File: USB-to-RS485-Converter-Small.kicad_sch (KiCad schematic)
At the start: 21 parts, among them IC1 SN65HVD1782D, J1 Conn_01x02_Pin, J2 USB_B, J3 DE9_Plug_MountingHoles, U1 FT232RL

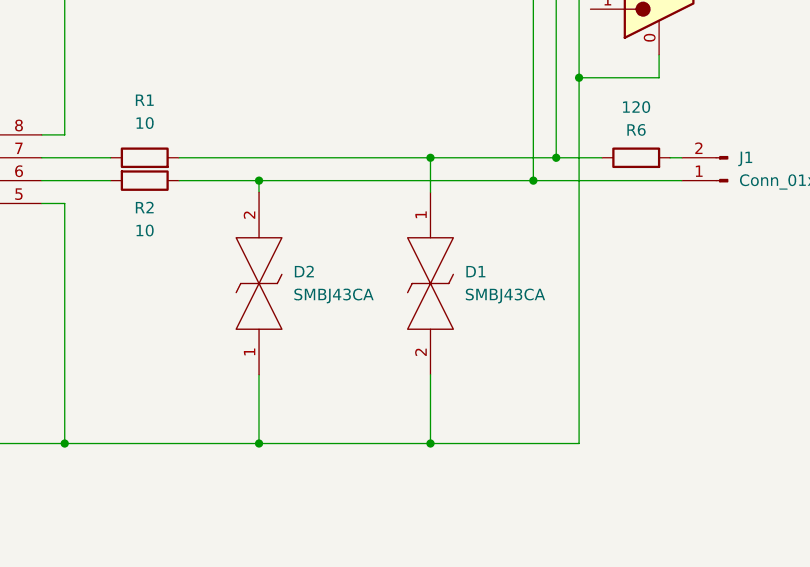
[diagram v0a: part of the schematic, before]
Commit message: Changed TVS diode
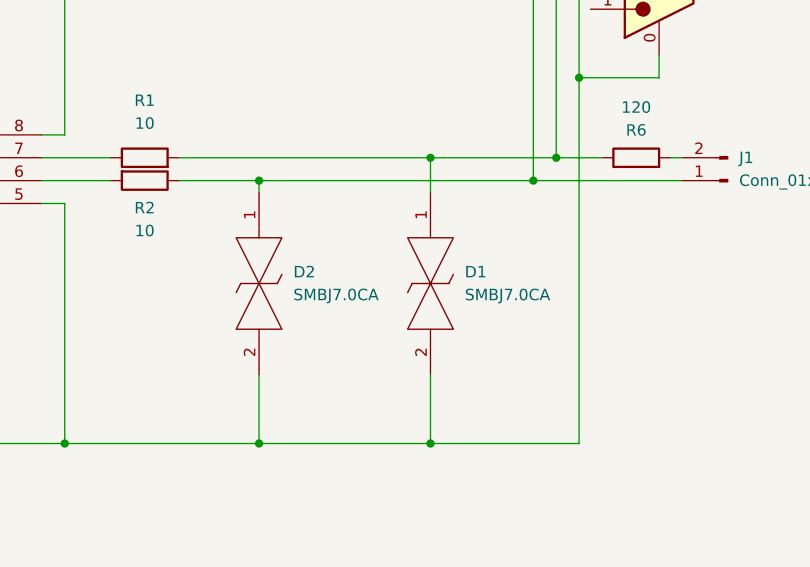
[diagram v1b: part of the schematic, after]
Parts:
- removed D1, D2: SMBJ43CA, DIONM5436X261N, symbol SamacSys_Parts:SMBJ43CA
- added D1, D2: SMBJ7.0CA, DIONM5436X261N, symbol SamacSys_Parts:SMBJ7.0CA
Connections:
- net GND: now also D1.2, D2.2
- net at J1.1 (Pin_1), J3.3, R2.1: now also D2.1
- net at J3.7, R1.2, R6.1: now also D1.1

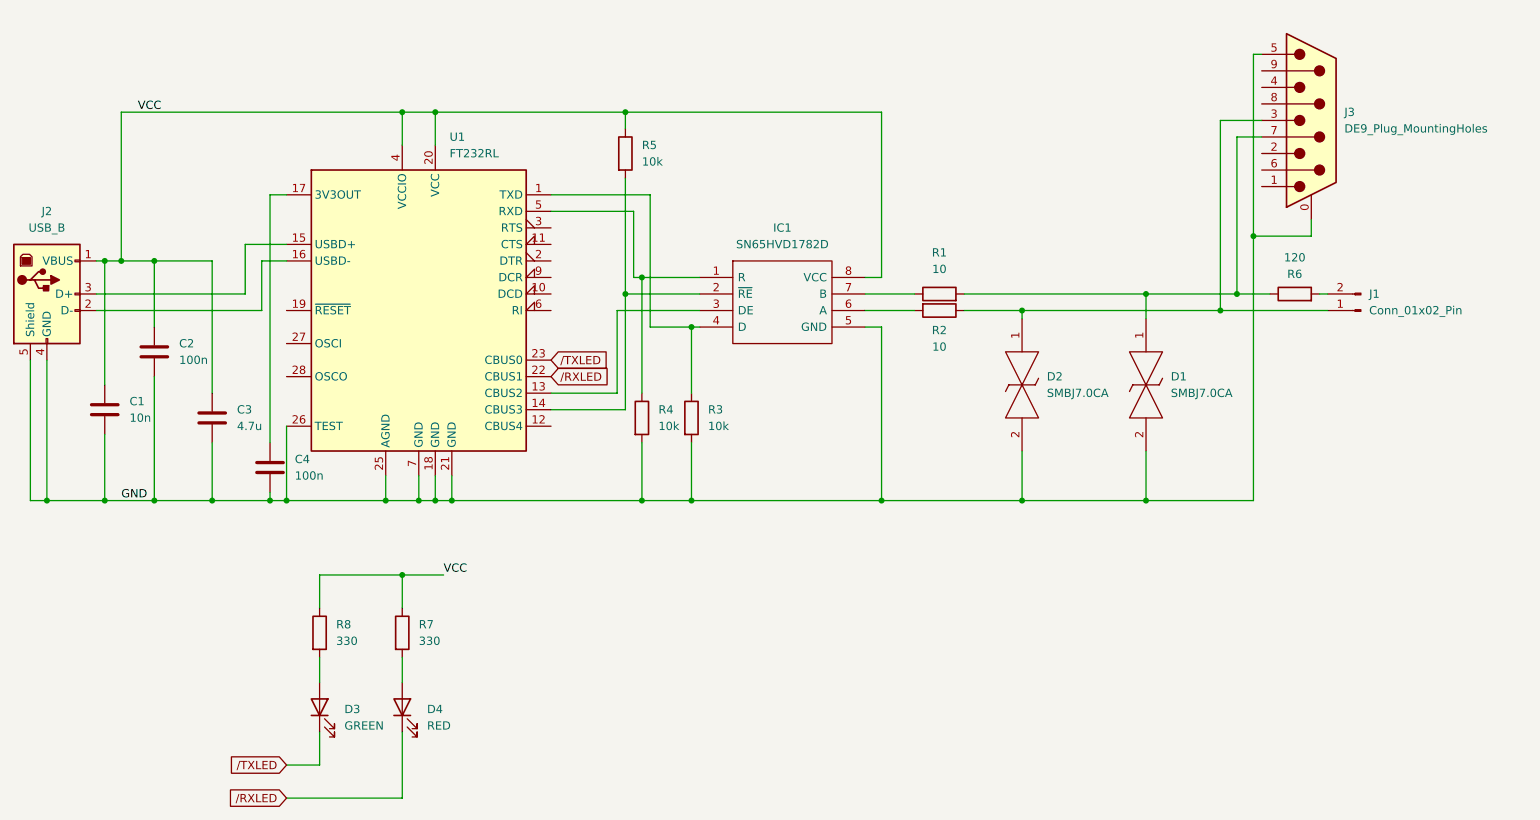
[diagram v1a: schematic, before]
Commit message: Changed RS485 transceiver and TVS diode
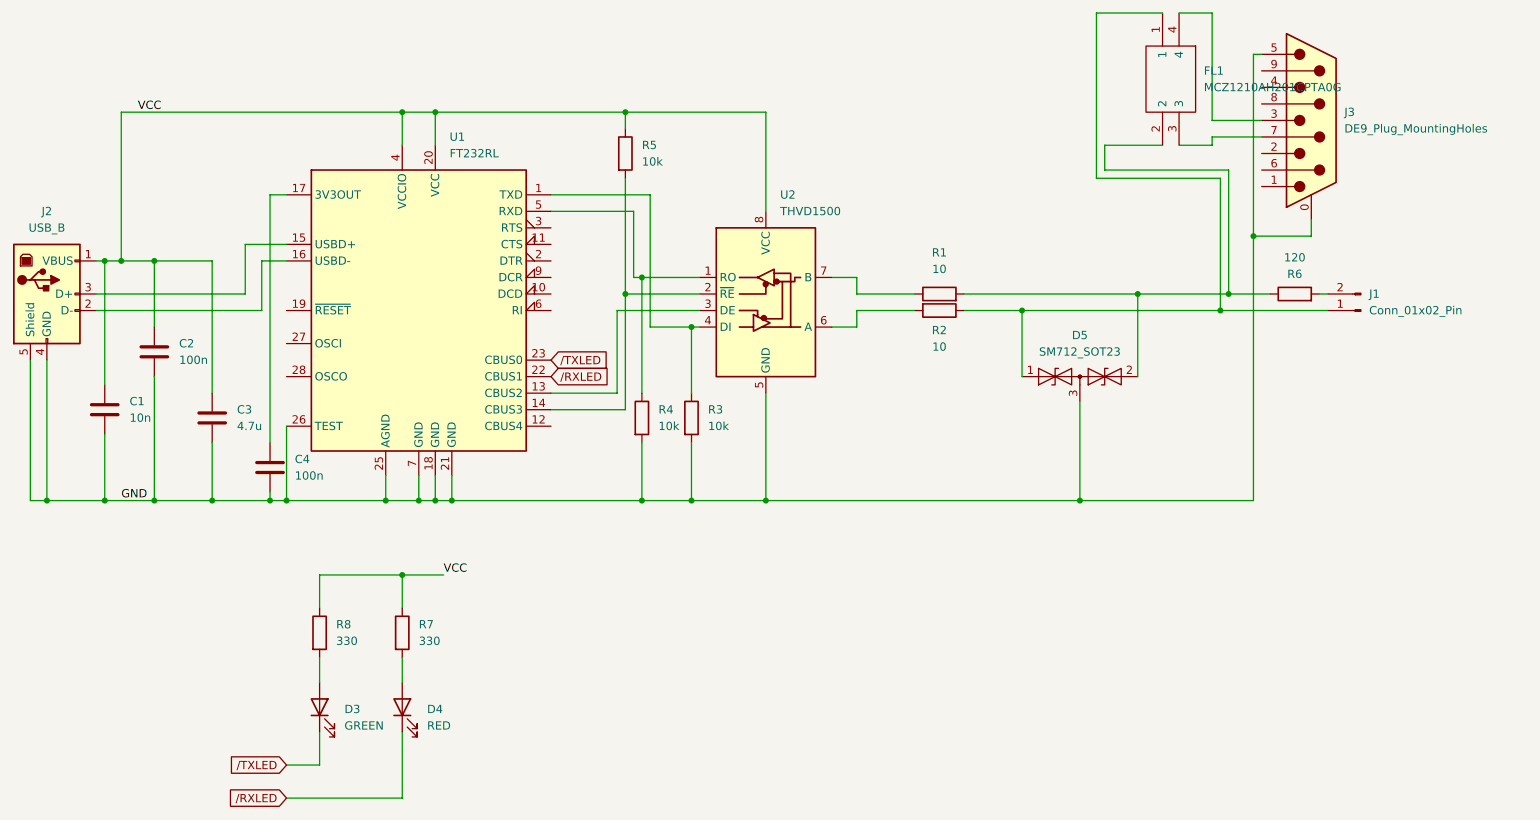
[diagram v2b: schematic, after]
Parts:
- removed D1, D2: SMBJ7.0CA, DIONM5436X261N, symbol SamacSys_Parts:SMBJ7.0CA
- removed IC1: SN65HVD1782D, SOIC127P600X175-8N, symbol SamacSys_Parts:SN65HVD1782D
- added D5: SM712_SOT23, Package_TO_SOT_SMD:SOT-23, symbol Diode:SM712_SOT23
- added FL1: MCZ1210AH201CPTA0G, MCZ1210AH201CPTA0G, symbol SamacSys_Parts:MCZ1210AH201CPTA0G
- added U2: THVD1500, Package_SO:SOIC-8_3.9x4.9mm_P1.27mm, symbol Interface_UART:THVD1500
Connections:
- net GND: now also D5.3 (common), U2.5 (GND)
- net VCC: now also U2.8 (VCC)
- net at J1.1 (Pin_1), R2.1: now also D5.1 (A1), FL1.1; no longer J3.3
- net at R1.2, R6.1: now also D5.2 (A2), FL1.2; no longer J3.7
- net at R1.1: now also U2.7 (B)
- net at R3.1, U1.1 (TXD): now also U2.4 (DI)
- net at U1.13 (CBUS2): now also U2.3 (DE)
- net at R5.2, U1.14 (CBUS3): now also U2.2 (~{RE})
- net at R4.1, U1.5 (RXD): now also U2.1 (RO)
- net at R2.2: now also U2.6 (A)
- new net: FL1.4, J3.3
- new net: FL1.3, J3.7

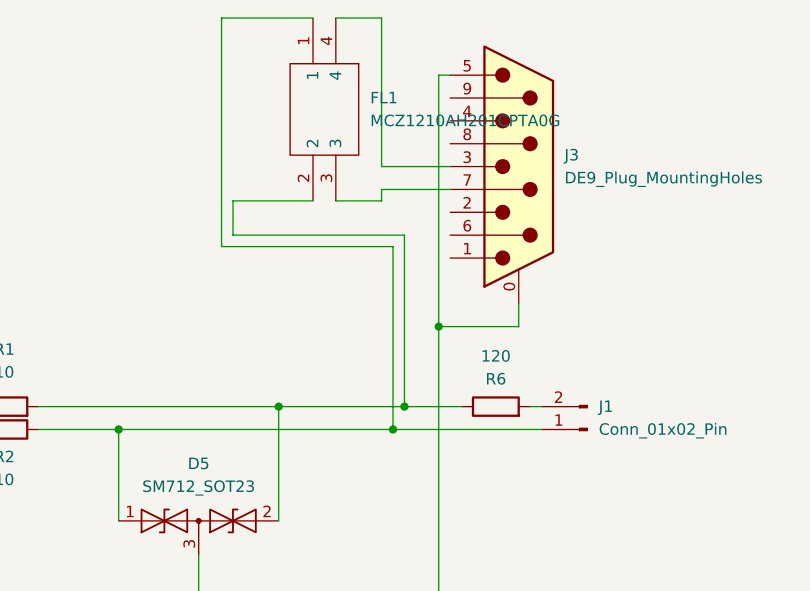
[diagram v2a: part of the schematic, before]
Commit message: Removed choke filter
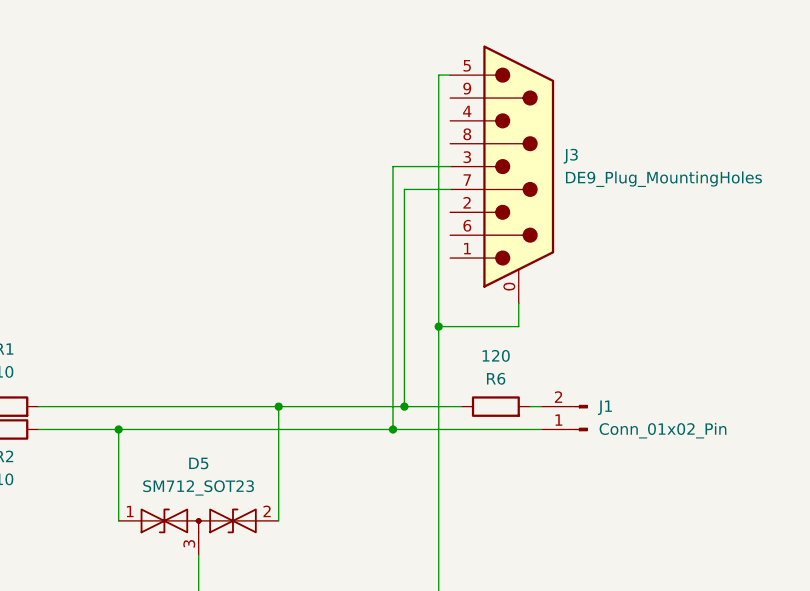
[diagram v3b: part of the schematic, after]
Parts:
- removed FL1: MCZ1210AH201CPTA0G, MCZ1210AH201CPTA0G, symbol SamacSys_Parts:MCZ1210AH201CPTA0G
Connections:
- net at J3.3: now also D5.1 (A1), J1.1 (Pin_1), R2.1
- net at J3.7: now also D5.2 (A2), R1.2, R6.1
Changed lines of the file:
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@@
 	(wire
 		(pts
-			(xy 222.25 48.26) (xy 212.09 48.26)
+			(xy 231.14 64.77) (xy 237.49 64.77)
 		)
 		(stroke
@@
 	(wire
 		(pts
-			(xy 212.09 73.66) (xy 231.14 73.66)
-		)
-		(stroke
-			(width 0)
-			(type default)
-		)
-	)
-	(wire
-		(pts
 			(xy 149.86 123.19) (xy 161.29 123.19)
 		)
@@
 	(wire
 		(pts
-			(xy 229.87 67.31) (xy 229.87 68.58)
-		)
-		(stroke
-			(width 0)
-			(type default)
-		)
-	)
-	(wire
-		(pts
 			(xy 105.41 134.62) (xy 105.41 139.7)
 		)
@@
 	(wire
 		(pts
-			(xy 229.87 64.77) (xy 237.49 64.77)
-		)
-		(stroke
-			(width 0)
-			(type default)
-		)
-	)
-	(wire
-		(pts
 			(xy 138.43 106.68) (xy 138.43 93.98)
 		)
@@
 	(wire
 		(pts
-			(xy 213.36 68.58) (xy 213.36 72.39)
-		)
-		(stroke
-			(width 0)
-			(type default)
-		)
-	)
-	(wire
-		(pts
 			(xy 110.49 63.5) (xy 139.7 63.5)
 		)
@@
 	(wire
 		(pts
-			(xy 212.09 48.26) (xy 212.09 73.66)
+			(xy 231.14 64.77) (xy 231.14 93.98)
 		)
 		(stroke
@@
 	(wire
 		(pts
-			(xy 229.87 68.58) (xy 224.79 68.58)
-		)
-		(stroke
-			(width 0)
-			(type default)
-		)
-	)
-	(wire
-		(pts
 			(xy 92.71 139.7) (xy 92.71 134.62)
 		)
@@
 	(wire
 		(pts
-			(xy 231.14 73.66) (xy 231.14 93.98)
-		)
-		(stroke
-			(width 0)
-			(type default)
-		)
-	)
-	(wire
-		(pts
 			(xy 245.11 80.01) (xy 245.11 82.55)
 		)
@@
 	(wire
 		(pts
-			(xy 229.87 48.26) (xy 229.87 64.77)
-		)
-		(stroke
-			(width 0)
-			(type default)
-		)
-	)
-	(wire
-		(pts
 			(xy 138.43 93.98) (xy 151.13 93.98)
 		)
@@
 	(wire
 		(pts
-			(xy 213.36 72.39) (xy 232.41 72.39)
-		)
-		(stroke
-			(width 0)
-			(type default)
-		)
-	)
-	(wire
-		(pts
 			(xy 59.69 113.03) (xy 59.69 123.19)
 		)
@@
 	(wire
 		(pts
-			(xy 232.41 72.39) (xy 232.41 91.44)
+			(xy 232.41 67.31) (xy 232.41 91.44)
 		)
 		(stroke
@@
 	(wire
 		(pts
-			(xy 224.79 48.26) (xy 229.87 48.26)
-		)
-		(stroke
-			(width 0)
-			(type default)
-		)
-	)
-	(wire
-		(pts
 			(xy 149.86 96.52) (xy 149.86 106.68)
 		)
@@
 	(wire
 		(pts
-			(xy 237.49 67.31) (xy 229.87 67.31)
-		)
-		(stroke
-			(width 0)
-			(type default)
-		)
-	)
-	(wire
-		(pts
 			(xy 142.24 88.9) (xy 151.13 88.9)
 		)
@@
 	(wire
 		(pts
-			(xy 213.36 68.58) (xy 222.25 68.58)
+			(xy 232.41 67.31) (xy 237.49 67.31)
 		)
 		(stroke
@@
 					(unit 1)
 				)
-			)
-		)
-	)
-	(symbol
-		(lib_id "SamacSys_Parts:MCZ1210AH201CPTA0G")
-		(at 224.79 48.26 270)
-		(unit 1)
-		(exclude_from_sim no)
-		(in_bom yes)
-		(on_board yes)
-		(dnp no)
-		(fields_autoplaced yes)
-		(property "Reference" "FL1"
-			(at 228.6 57.1499 90)
-			(effects
-				(font
-					(size 1.27 1.27)
-				)
-				(justify left)
-			)
-		)
-		(property "Value" "MCZ1210AH201CPTA0G"
-			(at 228.6 59.6899 90)
-			(effects
-				(font
-					(size 1.27 1.27)
-				)
-				(justify left)
-			)
-		)
-		(property "Footprint" "MCZ1210AH201CPTA0G"
-			(at 227.33 64.77 0)
-			(effects
-				(font
-					(size 1.27 1.27)
-				)
-				(justify left)
-				(hide yes)
-			)
-		)
-		(property "Datasheet" "https://product.tdk.com/system/files/dam/doc/product/emc/emc/cmf_cmc/catalog/cmf_commercial_signal_mcz1210ah_en.pdf"
-			(at 224.79 64.77 0)
-			(effects
-				(font
-					(size 1.27 1.27)
-				)
-				(justify left)
-				(hide yes)
-			)
-		)
-		(property "Description" "Common Mode Filters / Chokes, |Z|=200? at 100MHz."
-			(at 222.25 64.77 0)
-			(effects
-				(font
-					(size 1.27 1.27)
-				)
-				(justify left)
-				(hide yes)
-			)
-		)
-		(property "Height" "0.6"
-			(at 219.71 64.77 0)
-			(effects
-				(font
-					(size 1.27 1.27)
-				)
-				(justify left)
-				(hide yes)
-			)
-		)
-		(property "Mouser Part Number" "810-MCZ1210AH201CA0G"
-			(at 217.17 64.77 0)
-			(effects
-				(font
-					(size 1.27 1.27)
-				)
-				(justify left)
-				(hide yes)
-			)
-		)
-		(property "Mouser Price/Stock" "https://www.mouser.co.uk/ProductDetail/TDK/MCZ1210AH201CPTA0G?qs=MyNHzdoqoQJ4ZYwz7DkR6A%3D%3D"
-			(at 214.63 64.77 0)
-			(effects
-				(font
-					(size 1.27 1.27)
-				)
-				(justify left)
-				(hide yes)
-			)
-		)
-		(property "Manufacturer_Name" "TDK"
-			(at 212.09 64.77 0)
-			(effects
-				(font
-					(size 1.27 1.27)
-				)
-				(justify left)
-				(hide yes)
-			)
-		)
-		(property "Manufacturer_Part_Number" "MCZ1210AH201CPTA0G"
-			(at 209.55 64.77 0)
-			(effects
-				(font
-					(size 1.27 1.27)
-				)
-				(justify left)
-				(hide yes)
-			)
-		)
-		(pin "2"
-		)
-		(pin "4"
-		)
-		(pin "1"
-		)
-		(pin "3"
-		)
-		(instances
-			(project "USB-to-RS485-Converter-Small"
-				(path "/44eb492e-2114-45a2-84db-c63f5192c768"
-					(reference "FL1")
-					(unit 1)
-				)
